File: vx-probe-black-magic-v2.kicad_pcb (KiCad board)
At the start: 2 copper layers, 72.4 x 41.9 mm, 44 parts, among them P1 USB MINI B, P10 CONN_01X01, P11 CONN_01X11, P12 CONN_01X03, P2 +5v power input, P3 +5v external input, P4 CONN_02X05, P5 CONN_01X04, P6 swdio/jtag, P7 CONN_01X01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

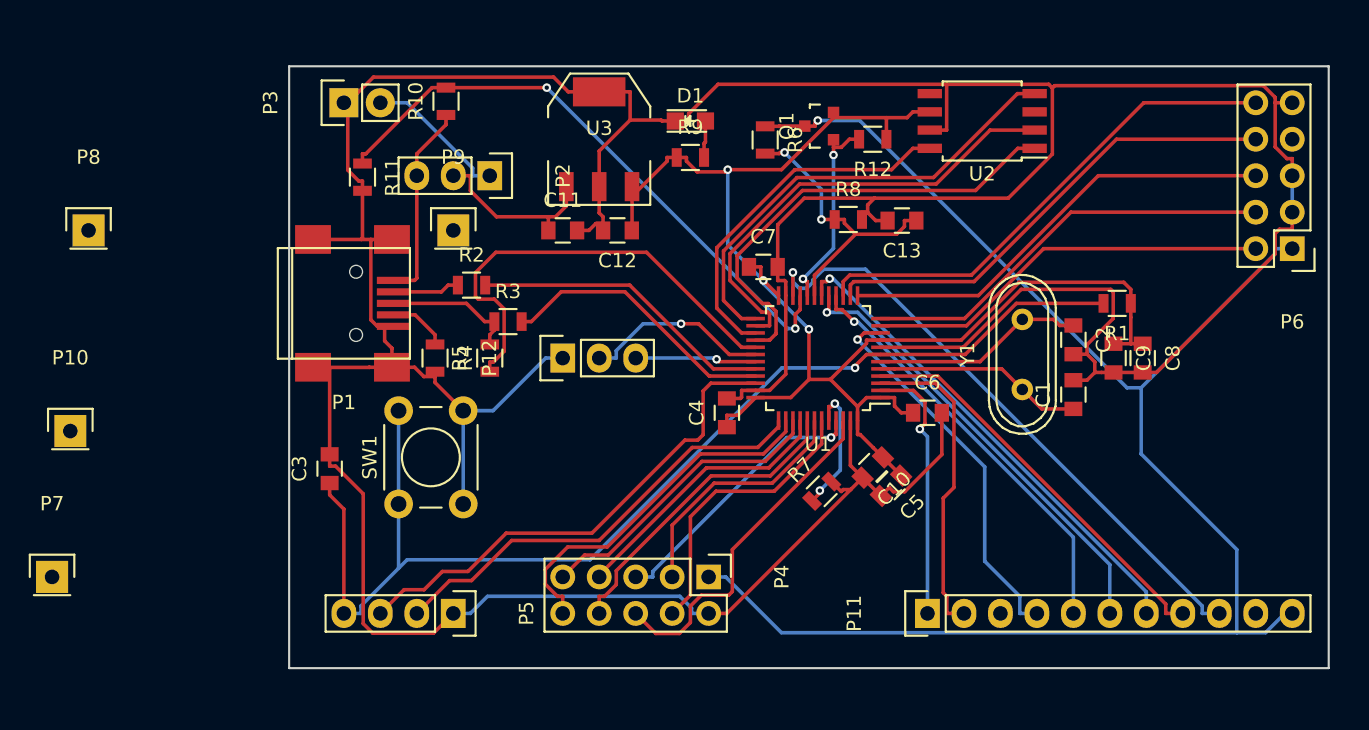
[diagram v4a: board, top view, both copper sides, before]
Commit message: changed the jtag and uext connectors to idc headers
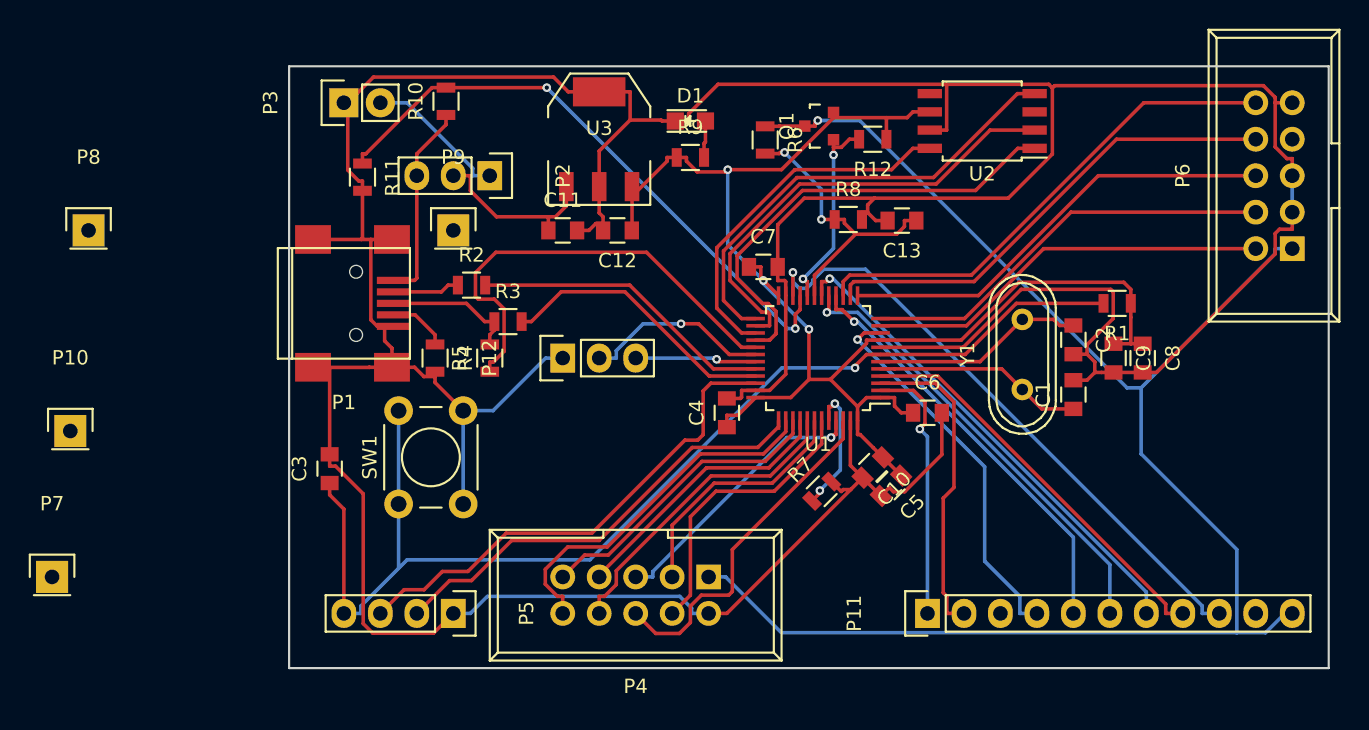
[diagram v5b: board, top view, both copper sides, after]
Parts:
- P4, P6: footprint Pin_Headers:Pin_Header_Straight_2x05 -> Connect:IDC_Header_Straight_10pins
- turned P4 to 180 degrees
- turned P6 to 90 degrees

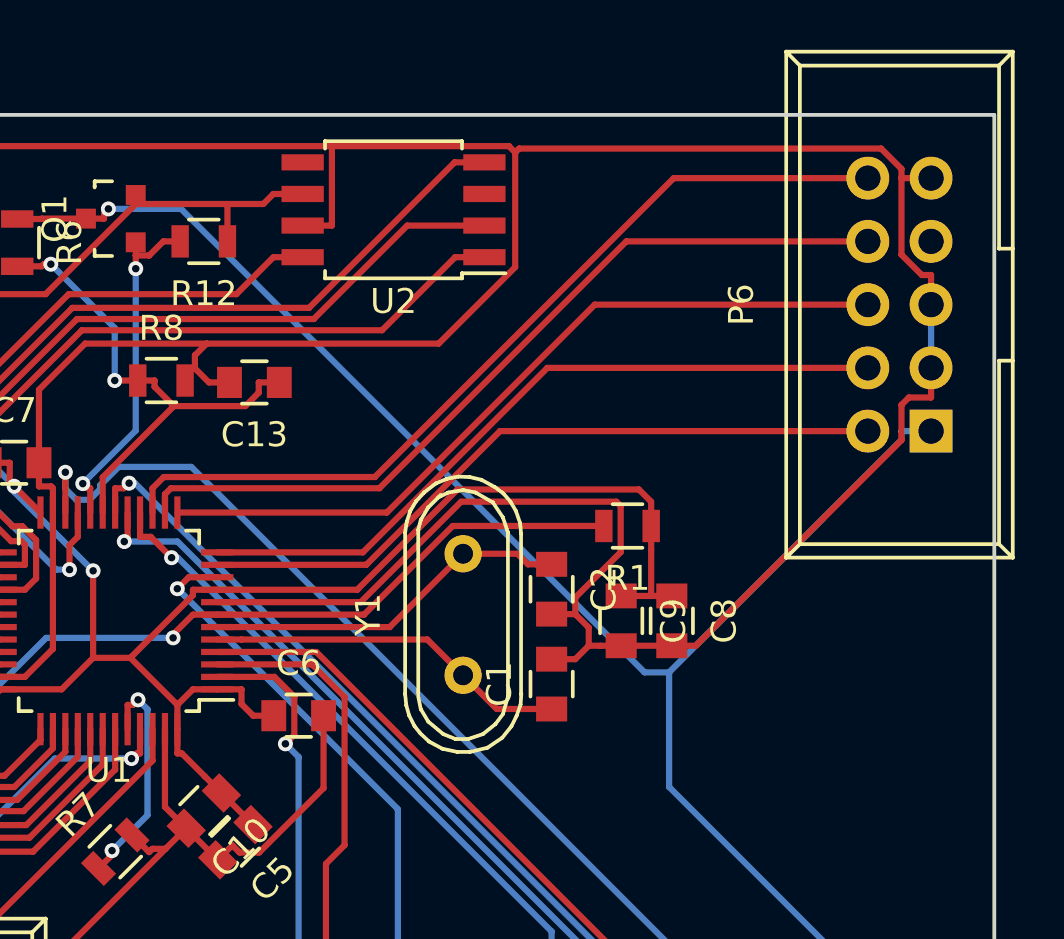
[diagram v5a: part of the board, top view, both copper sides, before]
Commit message: displaced the jtag connector
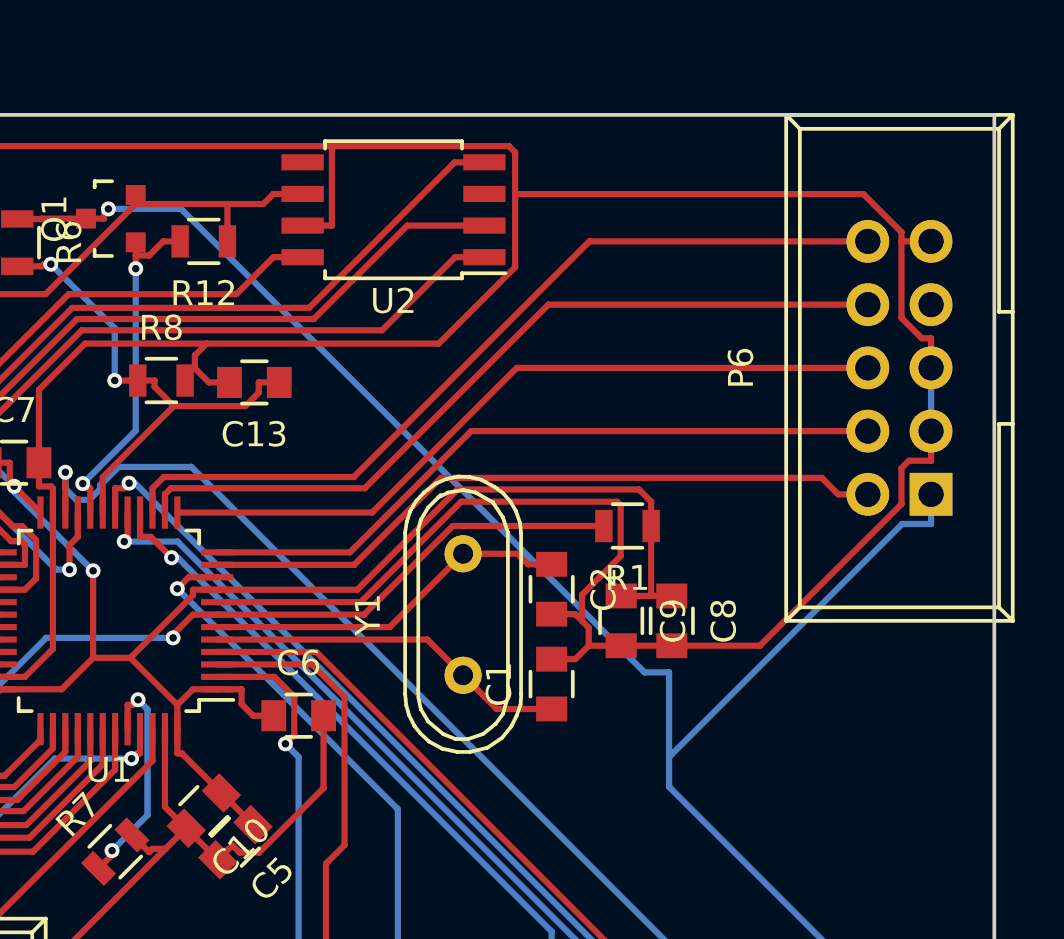
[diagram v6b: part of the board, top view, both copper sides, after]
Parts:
- moved P6 2.54 mm to (116.8, 54.6)
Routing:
- net /TDI: track 33.3 -> 32.1 mm
- net /SWO/TDO: track 31.3 -> 30.1 mm
- net /SWCLK/TCK: track 29.2 -> 28.1 mm
- net /XRST: track 34.9 -> 33.8 mm
- net /TPWR: track 111.5 -> 112.4 mm
- net GND: track 317.9 -> 317.2 mm
- net /SWDIO/TMS: track 28.4 -> 27.9 mm

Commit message: bundled the jtag signals closer together
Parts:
- moved P7 8.64 mm to (30.8, 66.3)
- moved P10 5.34 mm to (33.7, 59.8)
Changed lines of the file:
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@@
   (general
     (links 119)
-    (no_connects 0)
-    (area 46.914999 39.294999 119.455001 81.355001)
+    (no_connects 1)
+    (area 20.219999 24.029999 271.880001 161.390001)
     (thickness 1.6)
     (drawings 11)
-    (tracks 570)
+    (tracks 574)
     (zones 0)
     (modules 44)
@@
   )
   (module Pin_Headers:Pin_Header_Straight_1x01 (layer F.Cu)
-    (at 30.48 74.93)
+    (at 30.8 66.3)
     (descr "Through hole pin header")
     (tags "pin header")
@@
   )
   (module Pin_Headers:Pin_Header_Straight_1x01 (layer F.Cu)
-    (at 31.75 64.77)
+    (at 33.7 59.8)
     (descr "Through hole pin header")
     (tags "pin header")
@@
   (segment (start 113.111 54.61) (end 112.448 53.9464) (width 0.25) (layer F.Cu) (net 32))
   (segment (start 114.3 54.61) (end 113.111 54.61) (width 0.25) (layer F.Cu) (net 32))
-  (segment (start 93.4987 56.94) (end 88.17 56.94) (width 0.25) (layer F.Cu) (net 33))
-  (segment (start 98.3687 52.07) (end 93.4987 56.94) (width 0.25) (layer F.Cu) (net 33))
-  (segment (start 114.3 52.07) (end 98.3687 52.07) (width 0.25) (layer F.Cu) (net 33))
-  (segment (start 100.201 49.53) (end 114.3 49.53) (width 0.25) (layer F.Cu) (net 34))
-  (segment (start 94.3913 55.34) (end 100.201 49.53) (width 0.25) (layer F.Cu) (net 34))
-  (segment (start 86.57 55.34) (end 94.3913 55.34) (width 0.25) (layer F.Cu) (net 34))
-  (segment (start 86.07 54.6049) (end 86.07 55.34) (width 0.25) (layer F.Cu) (net 36))
-  (segment (start 86.3102 54.3647) (end 86.07 54.6049) (width 0.25) (layer F.Cu) (net 36))
-  (segment (start 94.0929 54.3647) (end 86.3102 54.3647) (width 0.25) (layer F.Cu) (net 36))
-  (segment (start 101.468 46.99) (end 94.0929 54.3647) (width 0.25) (layer F.Cu) (net 36))
-  (segment (start 114.3 46.99) (end 101.468 46.99) (width 0.25) (layer F.Cu) (net 36))
+  (segment (start 113.111 52.07) (end 114.3 52.07) (width 0.25) (layer F.Cu) (net 33))
+  (segment (start 111.685 53.496) (end 113.111 52.07) (width 0.25) (layer F.Cu) (net 33))
+  (segment (start 92.5893 53.496) (end 111.685 53.496) (width 0.25) (layer F.Cu) (net 33))
+  (segment (start 89.1453 56.94) (end 92.5893 53.496) (width 0.25) (layer F.Cu) (net 33))
+  (segment (start 88.17 56.94) (end 89.1453 56.94) (width 0.25) (layer F.Cu) (net 33))
+  (segment (start 113.111 49.53) (end 114.3 49.53) (width 0.25) (layer F.Cu) (net 34))
+  (segment (start 109.595 53.0457) (end 113.111 49.53) (width 0.25) (layer F.Cu) (net 34))
+  (segment (start 88.8643 53.0457) (end 109.595 53.0457) (width 0.25) (layer F.Cu) (net 34))
+  (segment (start 86.57 55.34) (end 88.8643 53.0457) (width 0.25) (layer F.Cu) (net 34))
+  (segment (start 86.07 54.5016) (end 86.07 55.34) (width 0.25) (layer F.Cu) (net 36))
+  (segment (start 88.0231 52.5485) (end 86.07 54.5016) (width 0.25) (layer F.Cu) (net 36))
+  (segment (start 107.553 52.5485) (end 88.0231 52.5485) (width 0.25) (layer F.Cu) (net 36))
+  (segment (start 113.111 46.99) (end 107.553 52.5485) (width 0.25) (layer F.Cu) (net 36))
+  (segment (start 114.3 46.99) (end 113.111 46.99) (width 0.25) (layer F.Cu) (net 36))
   (segment (start 85.57 54.3647) (end 85.57 55.34) (width 0.25) (layer F.Cu) (net 37))
-  (segment (start 86.0203 53.9144) (end 85.57 54.3647) (width 0.25) (layer F.Cu) (net 37))
-  (segment (start 93.653 53.9144) (end 86.0203 53.9144) (width 0.25) (layer F.Cu) (net 37))
-  (segment (start 103.117 44.45) (end 93.653 53.9144) (width 0.25) (layer F.Cu) (net 37))
-  (segment (start 114.3 44.45) (end 103.117 44.45) (width 0.25) (layer F.Cu) (net 37))
+  (segment (start 87.8399 52.0948) (end 85.57 54.3647) (width 0.25) (layer F.Cu) (net 37))
+  (segment (start 105.838 52.0948) (end 87.8399 52.0948) (width 0.25) (layer F.Cu) (net 37))
+  (segment (start 113.111 44.8215) (end 105.838 52.0948) (width 0.25) (layer F.Cu) (net 37))
+  (segment (start 113.111 44.45) (end 113.111 44.8215) (width 0.25) (layer F.Cu) (net 37))
+  (segment (start 114.3 44.45) (end 113.111 44.45) (width 0.25) (layer F.Cu) (net 37))
   (via (at 82.7694 54.1783) (size 0.6) (layers F.Cu B.Cu) (net 38))
   (via (at 84.897 45.5458) (size 0.6) (layers F.Cu B.Cu) (net 38))
